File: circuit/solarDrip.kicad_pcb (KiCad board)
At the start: 2 copper layers, 57 x 50 mm, 44 parts, among them J1 solar_charger, J10 Conn_01x08_Socket, J2 batt, J3 solar, J4 pump, J5 soil, J6 water, J7 USB_C_Receptacle_USB2.0_14P, J8 i2c, J9 Conn_01x08_Socket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

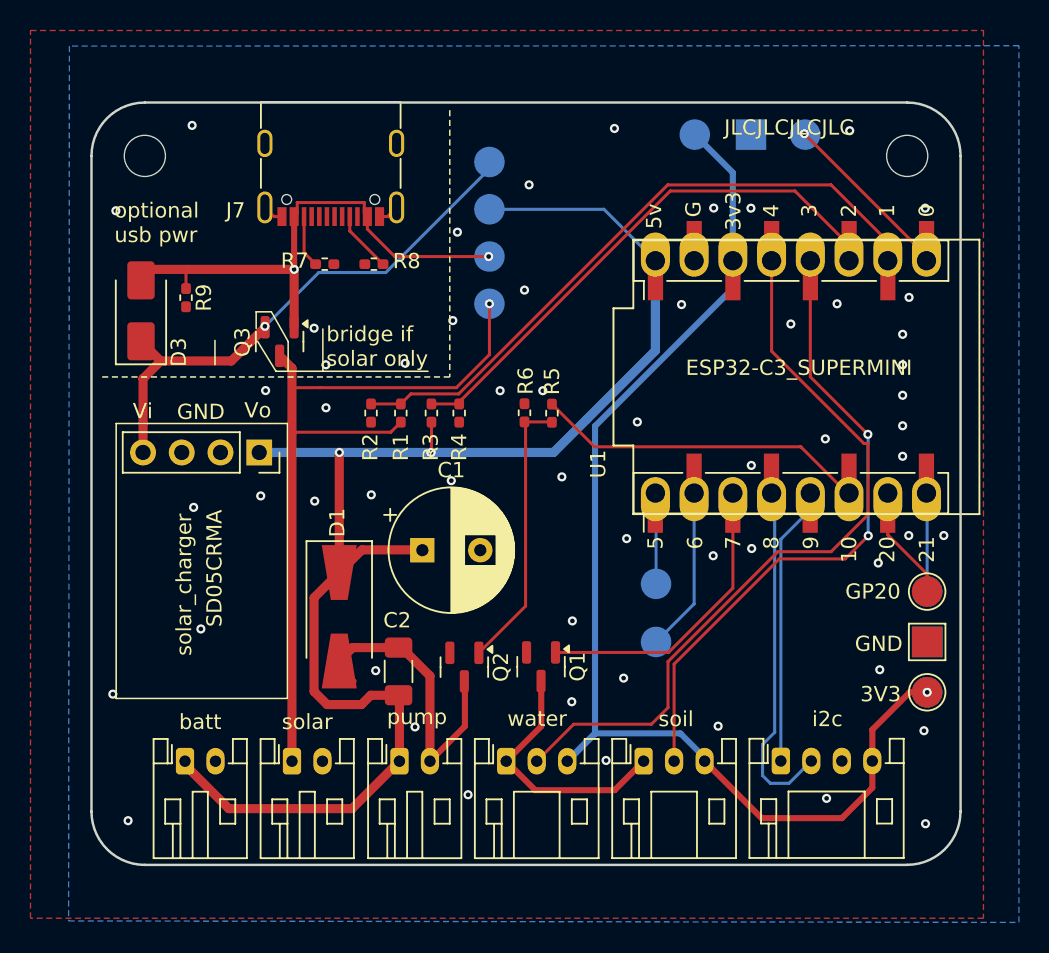
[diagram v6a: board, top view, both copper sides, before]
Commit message: add sensor pypass caps
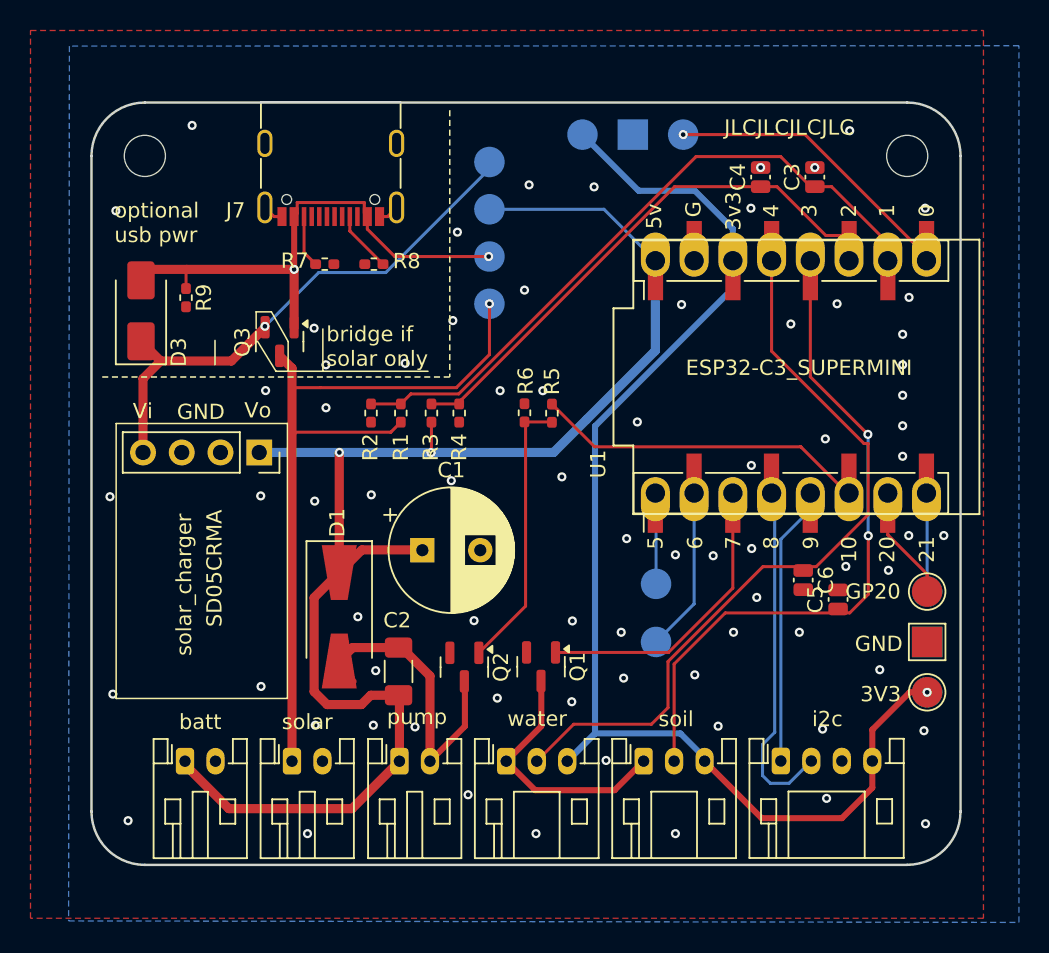
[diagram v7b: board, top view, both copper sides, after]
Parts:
- added C3: 100nF, Capacitor_SMD:C_0504_1310Metric_Pad0.83x1.28mm_HandSolder, F.Cu at (68.2, 43.4)
- added C4: 100nF, Capacitor_SMD:C_0504_1310Metric_Pad0.83x1.28mm_HandSolder, F.Cu at (64.6, 43.4)
- added C5: 100nF, Capacitor_SMD:C_0504_1310Metric_Pad0.83x1.28mm_HandSolder, F.Cu at (69.7, 71.1)
- added C6: 100nF, Capacitor_SMD:C_0504_1310Metric_Pad0.83x1.28mm_HandSolder, F.Cu at (67.4, 69.8)
- C1: value C_Polarized -> 330µF
- C2: value C -> 1µF
- moved TP10 8.00 mm to (59.6, 40.6)
- moved TP7 7.75 mm to (56.3, 40.6)
- moved TP6 7.37 mm to (53.0, 40.6)
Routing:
- net gpio0: track 11.7 -> 19.6 mm
- net vcc_logic: track 79.1 -> 84.3 mm
- net solar_hi: track 42.6 -> 45.4 mm
- net in-a_moisture: track 42.2 -> 44.5 mm
- net GND: vias 57 -> 74

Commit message: add artwork: dripbot & mc3 logo
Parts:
- added J11: Conn_01x01_Pin, my_footprints:logo_solardrip, B.Cu at (31.1, 78.7)
- moved TP3 1.61 mm to (46.1, 41.0)
- moved TP1 1.43 mm to (46.1, 44.3)
- moved TP15 1.26 mm to (46.1, 47.6)
- moved TP2 1.11 mm to (46.1, 50.9)
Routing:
- net vcc_battery: track 98.8 -> 99.9 mm
